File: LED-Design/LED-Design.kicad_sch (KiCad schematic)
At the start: 162 parts, among them Q1 NMOS, Q2 NMOS, Q3 NMOS, Q4 NMOS, Q5 NMOS, Q6 NMOS, Q7 NMOS, U1 74LS573, U2 74LS573, U3 74LS573, U4 74LS573, U5 74HC164

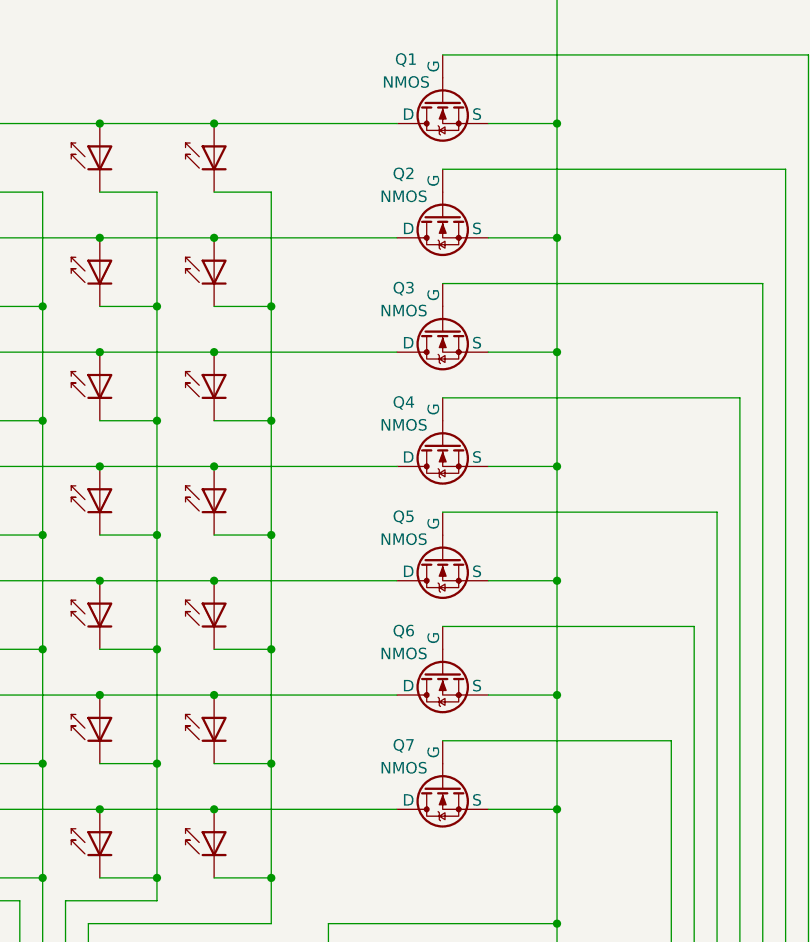
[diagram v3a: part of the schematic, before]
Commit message: Fixed the assignment of the MOSFET footprints to be GDS.
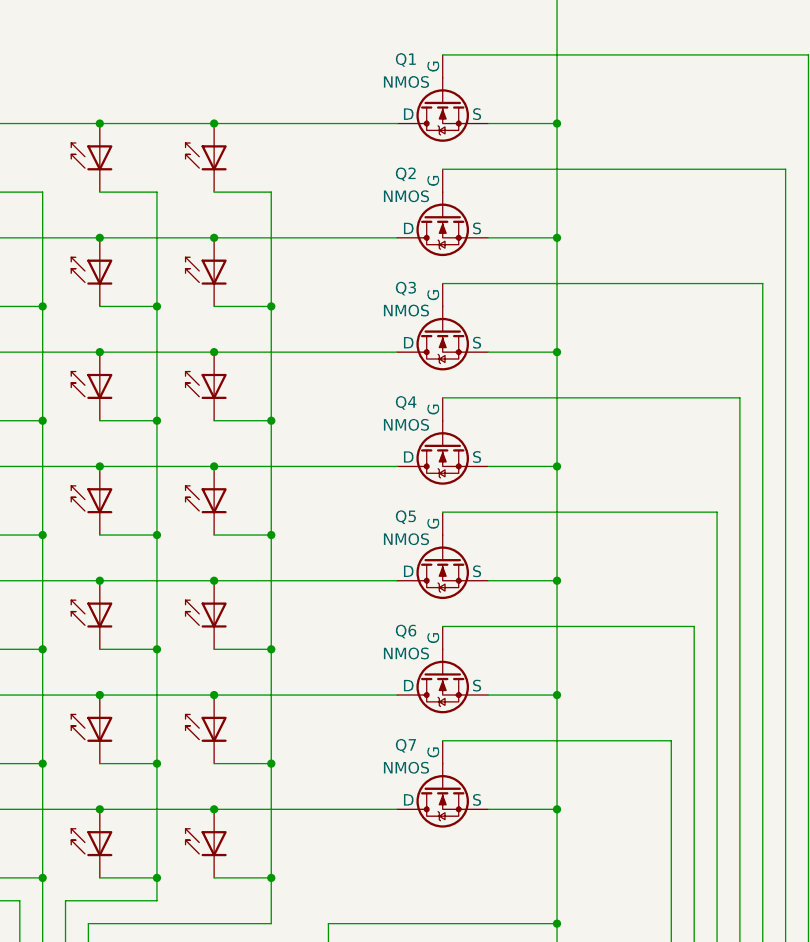
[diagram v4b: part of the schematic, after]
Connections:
- net at D102.2 (A), D109.2 (A), D11.2 (A)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: now also Q4.2 (D); no longer Q4.1 (D)
- net at D1.2 (A), D106.2 (A), D113.2 (A)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: now also Q1.2 (D); no longer Q1.1 (D)
- net at D104.2 (A), D111.2 (A), D118.2 (A)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: now also Q6.2 (D); no longer Q6.1 (D)
- net at D103.2 (A), D110.2 (A), D117.2 (A)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: now also Q5.2 (D); no longer Q5.1 (D)
- net at D10.2 (A), D101.2 (A), D108.2 (A)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: now also Q3.2 (D); no longer Q3.1 (D)
- net at U5.5 (Q2): now also Q3.1 (G); no longer Q3.2 (G)
- net at D100.2 (A), D107.2 (A), D114.2 (A)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: now also Q2.2 (D); no longer Q2.1 (D)
- net at D105.2 (A), D112.2 (A), D119.2 (A)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: now also Q7.2 (D); no longer Q7.1 (D)
- net at U5.10 (Q4): now also Q5.1 (G); no longer Q5.2 (G)
- net at U5.11 (Q5): now also Q6.1 (G); no longer Q6.2 (G)
- net at U5.12 (Q6): now also Q7.1 (G); no longer Q7.2 (G)
- net at U5.3 (Q0): now also Q1.1 (G); no longer Q1.2 (G)
- net at U5.4 (Q1): now also Q2.1 (G); no longer Q2.2 (G)
- net at U5.6 (Q3): now also Q4.1 (G); no longer Q4.2 (G)

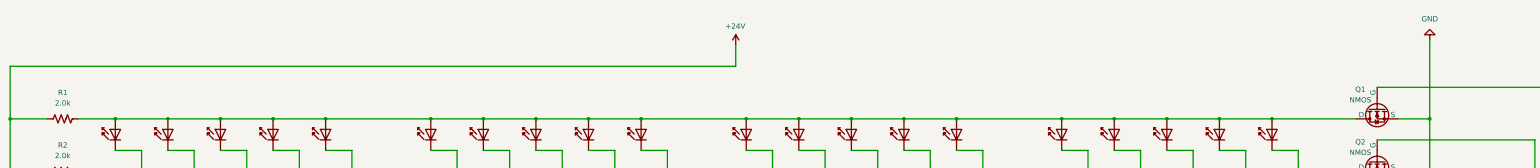
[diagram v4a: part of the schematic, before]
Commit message: Added footprints for ground and power
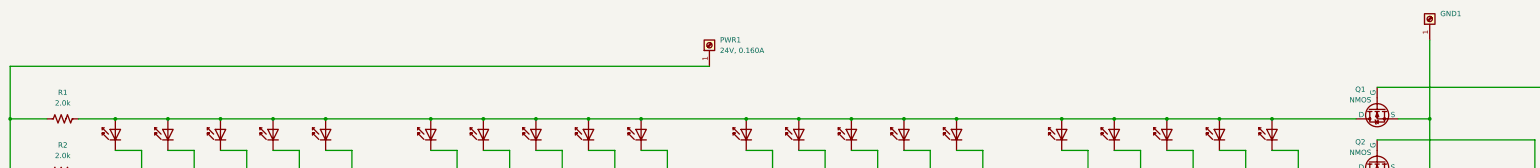
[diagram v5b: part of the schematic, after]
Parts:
- added GND1: ~, TerminalBlock_MetzConnect:TerminalBlock_MetzConnect_360271_1x01_Horizontal_ScrewM3.0_Boxed, symbol Connector:Screw_Terminal_01x01
- added PWR1: 24V, 0.160A, TerminalBlock_MetzConnect:TerminalBlock_MetzConnect_360271_1x01_Horizontal_ScrewM3.0_Boxed, symbol Connector:Screw_Terminal_01x01
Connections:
- net +24V: no longer names the net of R1.1, R2.1, R3.1, R4.1, R5.1, R6.1, R7.1, R8.1
- net +24V: now also PWR1.1 (Pin_1)
- net GND: no longer names the net of A1.29 (GND), Q1.3 (S), Q2.3 (S), Q3.3 (S), Q4.3 (S), Q5.3 (S), Q6.3 (S), Q7.3 (S), R9.2, U1.1 (~{OE}), U1.10 (GND), U2.1 (~{OE}), U2.10 (GND), U3.1 (~{OE}), U3.10 (GND), U4.1 (~{OE}), U4.10 (GND), U5.7 (GND)
- net GND: now also GND1.1 (Pin_1)
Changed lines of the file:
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@@
 	(wire
 		(pts
-			(xy 25.4 38.1) (xy 200.66 38.1)
+			(xy 25.4 38.1) (xy 194.31 38.1)
 		)
 		(stroke
@@
 	(wire
 		(pts
-			(xy 200.66 33.02) (xy 200.66 38.1)
-		)
-		(stroke
-			(width 0)
-			(type default)
-		)
-	)
-	(wire
-		(pts
 			(xy 285.75 109.22) (xy 285.75 121.92)
 		)
@@
 	)
 	(symbol
+		(lib_id "Connector:Screw_Terminal_01x01")
+		(at 194.31 33.02 90)
+		(unit 1)
+		(exclude_from_sim no)
+		(in_bom yes)
+		(on_board yes)
+		(dnp no)
+		(fields_autoplaced yes)
+		(property "Reference" "PWR1"
+			(at 196.85 31.7499 90)
+			(effects
+				(font
+					(size 1.27 1.27)
+				)
+				(justify right)
+			)
+		)
+		(property "Value" "24V, 0.160A"
+			(at 196.85 34.2899 90)
+			(effects
+				(font
+					(size 1.27 1.27)
+				)
+				(justify right)
+			)
+		)
+		(property "Footprint" "TerminalBlock_MetzConnect:TerminalBlock_MetzConnect_360271_1x01_Horizontal_ScrewM3.0_Boxed"
+			(at 194.31 33.02 0)
+			(effects
+				(font
+					(size 1.27 1.27)
+				)
+				(hide yes)
+			)
+		)
+		(property "Datasheet" "~"
+			(at 194.31 33.02 0)
+			(effects
+				(font
+					(size 1.27 1.27)
+				)
+				(hide yes)
+			)
+		)
+		(property "Description" "Generic screw terminal, single row, 01x01, script generated (kicad-library-utils/schlib/autogen/connector/)"
+			(at 194.31 33.02 0)
+			(effects
+				(font
+					(size 1.27 1.27)
+				)
+				(hide yes)
+			)
+		)
+		(pin "1"
+		)
+		(instances
+			(project "LED-Design"
+				(path "/f4f73743-e943-40e7-b3a9-52df178c6ab8"
+					(reference "PWR1")
+					(unit 1)
+				)
+			)
+		)
+	)
+	(symbol
 		(lib_name "NMOS_1")
 		(lib_id "Simulation_SPICE:NMOS")
@@
 	)
 	(symbol
-		(lib_id "power:+24V")
-		(at 200.66 33.02 0)
-		(unit 1)
-		(exclude_from_sim no)
-		(in_bom yes)
-		(on_board yes)
-		(dnp no)
-		(property "Reference" "#PWR01"
-			(at 200.66 36.83 0)
-			(effects
-				(font
-					(size 1.27 1.27)
-				)
-				(hide yes)
-			)
-		)
-		(property "Value" "+24V"
-			(at 198.12 28.448 0)
-			(effects
-				(font
-					(size 1.27 1.27)
-				)
-				(justify left)
-			)
-		)
-		(property "Footprint" ""
-			(at 200.66 33.02 0)
-			(effects
-				(font
-					(size 1.27 1.27)
-				)
-				(hide yes)
-			)
-		)
-		(property "Datasheet" ""
-			(at 200.66 33.02 0)
-			(effects
-				(font
-					(size 1.27 1.27)
-				)
-				(hide yes)
-			)
-		)
-		(property "Description" "Power symbol creates a global label with name \"+24V\""
-			(at 200.66 33.02 0)
-			(effects
-				(font
-					(size 1.27 1.27)
-				)
-				(hide yes)
-			)
-		)
-		(pin "1"
-		)
-		(instances
-			(project "LED-Design"
-				(path "/f4f73743-e943-40e7-b3a9-52df178c6ab8"
-					(reference "#PWR01")
-					(unit 1)
-				)
-			)
-		)
-	)
-	(symbol
 		(lib_id "LED:IR204A")
 		(at 254 129.54 90)
@@
 	)
 	(symbol
+		(lib_id "Connector:Screw_Terminal_01x01")
+		(at 368.3 26.67 90)
+		(unit 1)
+		(exclude_from_sim no)
+		(in_bom yes)
+		(on_board yes)
+		(dnp no)
+		(fields_autoplaced yes)
+		(property "Reference" "GND1"
+			(at 370.84 25.3999 90)
+			(effects
+				(font
+					(size 1.27 1.27)
+				)
+				(justify right)
+			)
+		)
+		(property "Value" "~"
+			(at 370.84 27.9399 90)
+			(effects
+				(font
+					(size 1.27 1.27)
+				)
+				(justify right)
+			)
+		)
+		(property "Footprint" "TerminalBlock_MetzConnect:TerminalBlock_MetzConnect_360271_1x01_Horizontal_ScrewM3.0_Boxed"
+			(at 368.3 26.67 0)
+			(effects
+				(font
+					(size 1.27 1.27)
+				)
+				(hide yes)
+			)
+		)
+		(property "Datasheet" "~"
+			(at 368.3 26.67 0)
+			(effects
+				(font
+					(size 1.27 1.27)
+				)
+				(hide yes)
+			)
+		)
+		(property "Description" "Generic screw terminal, single row, 01x01, script generated (kicad-library-utils/schlib/autogen/connector/)"
+			(at 368.3 26.67 0)
+			(effects
+				(font
+					(size 1.27 1.27)
+				)
+				(hide yes)
+			)
+		)
+		(pin "1"
+		)
+		(instances
+			(project "LED-Design"
+				(path "/f4f73743-e943-40e7-b3a9-52df178c6ab8"
+					(reference "GND1")
+					(unit 1)
+				)
+			)
+		)
+	)
+	(symbol
 		(lib_id "LED:IR204A")
 		(at 330.2 104.14 90)
@@
 					(unit 1)
 				)
-			)
-		)
-	)
-	(symbol
-		(lib_id "power:GND")
-		(at 368.3 31.75 180)
-		(unit 1)
-		(exclude_from_sim no)
-		(in_bom yes)
-		(on_board yes)
-		(dnp no)
-		(fields_autoplaced yes)
-		(property "Reference" "#PWR02"
-			(at 368.3 25.4 0)
-			(effects
-				(font
-					(size 1.27 1.27)
-				)
-				(hide yes)
-			)
-		)
-		(property "Value" "GND"
-			(at 368.3 26.67 0)
-			(effects
-				(font
-					(size 1.27 1.27)
-				)
-			)
-		)
-		(property "Footprint" ""
-			(at 368.3 31.75 0)
-			(effects
-				(font
-					(size 1.27 1.27)
-				)
-				(hide yes)
-			)
-		)
-		(property "Datasheet" ""
-			(at 368.3 31.75 0)
-			(effects
-				(font
-					(size 1.27 1.27)
-				)
-				(hide yes)
-			)
-		)
-		(property "Description" "Power symbol creates a global label with name \"GND\" , ground"
-			(at 368.3 31.75 0)
-			(effects
-				(font
-					(size 1.27 1.27)
-				)
-				(hide yes)
-			)
-		)
-		(pin "1"
-		)
-		(instances
-			(project "LED-Design"
-				(path "/f4f73743-e943-40e7-b3a9-52df178c6ab8"
-					(reference "#PWR02")
-					(unit 1)
-				)
